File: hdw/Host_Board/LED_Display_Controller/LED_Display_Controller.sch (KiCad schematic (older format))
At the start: 0 parts

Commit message: I said never do this, it's bad for you
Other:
- note added: "To Do List:\n* Add voltage rail ADC dividers/filters\n* ESD protection on input and output signals\n* Add graphical items to certain sheets (ESD warning, heat, etc)\n* Add MU Logo to each sheet\n* Add Titles to each sheet\n* Add relevant design notes/routing notes to sheets\n* Add test points sheet\n* Re-order sheets\n* Wire everything to Micro\n* Assign Refdes's\n* Draw custom footprints\n* Assi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"
- note removed: "To Do List:\n* Mechanical sheet\n* Decide on input power supply (AC/DC)\n* Add more power input connectors, match to AC/DC output connectors. Might need beefy Wuerth shanks\n* Add status LEDs, PGOOD stuff\n* +3.3V Power Supply (~~2A)\n* Add AUX +5V input if we mess up +5V supply\n* Wi-Fi Module\n* Evaluate Micro AVDD/AVSS filter\n* Power pushbutton? vs set on app?\n* Brightness encoder? vs set on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"
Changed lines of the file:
@@
 $Descr A 11000 8500
 encoding utf-8
-Sheet 1 32
+Sheet 1 31
 Title ""
 Date ""
@@
 F0 "Panel Data Connectors" 50
 F1 "Panel_Data_Connectors.sch" 50
-$EndSheet
-$Sheet
-S 3050 3270 500  150
-U 5BAAE2DF
-F0 "Panel Power Connectors" 50
-F1 "Panel_Power_Connectors.sch" 50
 $EndSheet
 $Sheet
@@
 $EndSheet
 Text Notes 710  7660 0    50   ~ 0
-To Do List:\n* Mechanical sheet\n* Decide on input power supply (AC/DC)\n* Add more power input connectors, match to AC/DC output connectors. Might need beefy Wuerth shanks\n* Add status LEDs, PGOOD stuff\n* +3.3V Power Supply (~~2A)\n* Add AUX +5V input if we mess up +5V supply\n* Wi-Fi Module\n* Evaluate Micro AVDD/AVSS filter\n* Power pushbutton? vs set on app?\n* Brightness encoder? vs set on app?\n* Add graphical items to certain sheets (ESD warning, heat, etc)\n* Add MU Logo to each sheet\n* Add Titles to each sheet\n* Add relevant design notes/routing notes to sheets\n* Add test points sheet\n* Re-order sheets\n* Wire everything to Micro\n* Assign Refdes's\n* Draw custom footprints\n* Assign footprints\n* Run ERC, resolve errors\n* Add firmware notes sheet\n* Add COM port settings note to USB sheet\n* Generate netlist\n* Generate BOM
+To Do List:\n* Add voltage rail ADC dividers/filters\n* ESD protection on input and output signals\n* Add graphical items to certain sheets (ESD warning, heat, etc)\n* Add MU Logo to each sheet\n* Add Titles to each sheet\n* Add relevant design notes/routing notes to sheets\n* Add test points sheet\n* Re-order sheets\n* Wire everything to Micro\n* Assign Refdes's\n* Draw custom footprints\n* Assign footprints\n* Assign Digi-Key Partnumbers\n* Run ERC, resolve errors\n* Add firmware notes sheet\n* Add COM port settings notes to USB sheet\n* Generate netlist\n* Generate BOM\n* Layout PCB
 $Sheet
 S 5450 5360 500  150
@@
 $EndSheet
 $Sheet
-S 7300 770  500  150
-U 5BC2370E
-F0 "POS5 Control" 50
-F1 "POS5_Control.sch" 50
+S 3050 3290 500  150
+U 5BE48F98
+F0 "LED POS5 Monitoring" 50
+F1 "LED_POS5_Monitoring.sch" 50
 $EndSheet
 $Sheet
-S 7300 1090 500  150
-U 5BC23711
-F0 "POS5 Phase 1" 50
-F1 "POS5_Phase_1.sch" 50
+S 5450 5700 500  150
+U 5BE4F849
+F0 "Pushbuttons" 50
+F1 "Pushbuttons.sch" 50
 $EndSheet
 $Sheet
-S 7300 1400 500  150
-U 5BC23715
-F0 "POS5 Phase 2" 50
-F1 "POS5_Phase_2.sch" 50
+S 5450 6040 500  150
+U 5BE5222A
+F0 "POS5 Power Supply" 50
+F1 "POS5_Power_Supply.sch" 50
 $EndSheet
 $Sheet
-S 7300 1740 500  150
-U 5BC2371A
-F0 "POS5 Phase 3" 50
-F1 "POS5_Phase_3.sch" 50
+S 7070 800  500  150
+U 5BE724F0
+F0 "Mechanical" 50
+F1 "Mechanical.sch" 50
 $EndSheet
 $Sheet
-S 7300 2060 500  150
-U 5BC2371D
-F0 "POS5 Phase 4" 50
-F1 "POS5_Phase_4.sch" 50
+S 7070 1140 500  150
+U 5BE7BB83
+F0 "Internal Rail Monitoring" 50
+F1 "Internal_Rail_Monitoring.sch" 50
 $EndSheet
 $Sheet
-S 7300 2430 500  150
-U 5BC23720
-F0 "POS5P5 MNG" 50
-F1 "POS5P5_MNG.sch" 50
+S 7070 1480 500  150
+U 5BF346B3
+F0 "Status LEDs 2" 50
+F1 "Status_LEDs_2.sch" 50
 $EndSheet
 $EndSCHEMATC

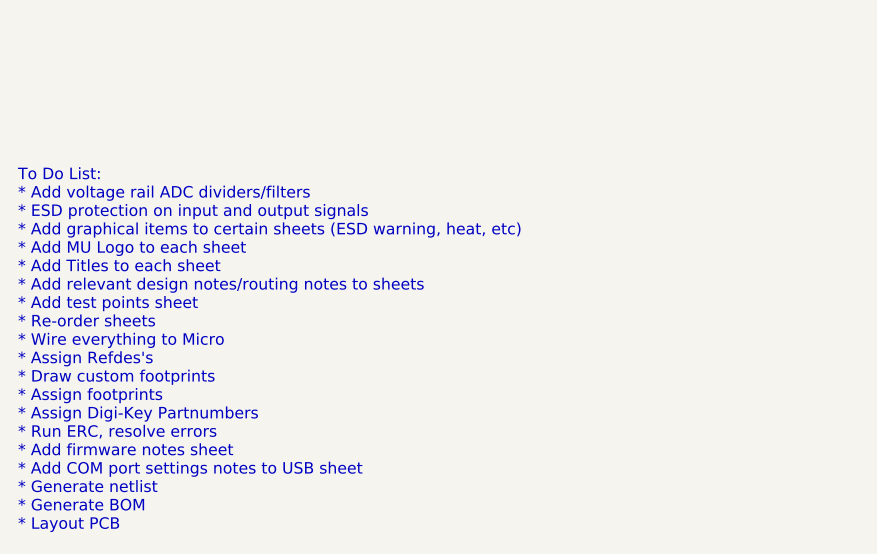
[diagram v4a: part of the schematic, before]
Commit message: Wired a lot of signals to micro, added COM port notes
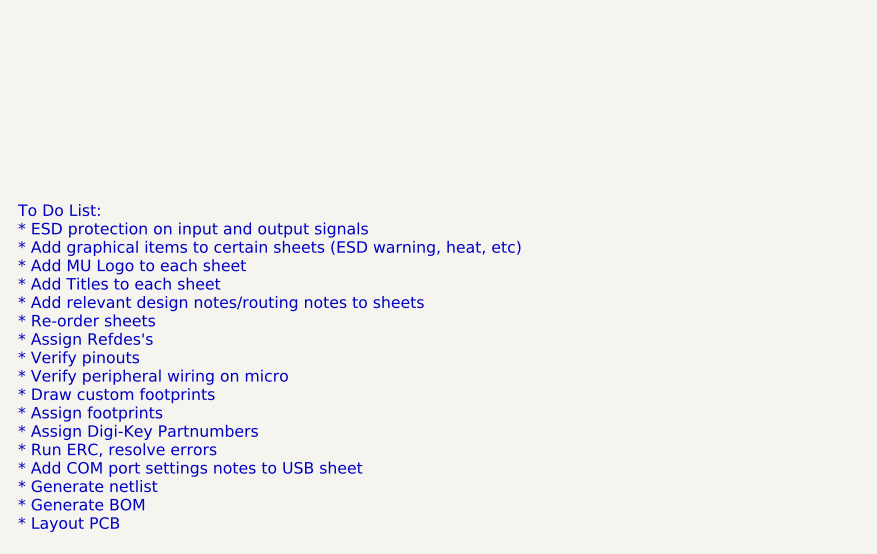
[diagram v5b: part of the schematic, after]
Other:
- note added: "To Do List:\n* ESD protection on input and output signals\n* Add graphical items to certain sheets (ESD warning, heat, etc)\n* Add MU Logo to each sheet\n* Add Titles to each sheet\n* Add relevant design notes/routing notes to sheets\n* Re-order sheets\n* Assign Refdes's\n* Verify pinouts\n* Verify peripheral wiring on micro\n* Draw custom footprints\n* Assign footprints\n* Assign Digi-Key Partnu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"
- note removed: "To Do List:\n* Add voltage rail ADC dividers/filters\n* ESD protection on input and output signals\n* Add graphical items to certain sheets (ESD warning, heat, etc)\n* Add MU Logo to each sheet\n* Add Titles to each sheet\n* Add relevant design notes/routing notes to sheets\n* Add test points sheet\n* Re-order sheets\n* Wire everything to Micro\n* Assign Refdes's\n* Draw custom footprints\n* Assi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"
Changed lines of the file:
@@
 $EndSheet
 Text Notes 710  7660 0    50   ~ 0
-To Do List:\n* Add voltage rail ADC dividers/filters\n* ESD protection on input and output signals\n* Add graphical items to certain sheets (ESD warning, heat, etc)\n* Add MU Logo to each sheet\n* Add Titles to each sheet\n* Add relevant design notes/routing notes to sheets\n* Add test points sheet\n* Re-order sheets\n* Wire everything to Micro\n* Assign Refdes's\n* Draw custom footprints\n* Assign footprints\n* Assign Digi-Key Partnumbers\n* Run ERC, resolve errors\n* Add firmware notes sheet\n* Add COM port settings notes to USB sheet\n* Generate netlist\n* Generate BOM\n* Layout PCB
+To Do List:\n* ESD protection on input and output signals\n* Add graphical items to certain sheets (ESD warning, heat, etc)\n* Add MU Logo to each sheet\n* Add Titles to each sheet\n* Add relevant design notes/routing notes to sheets\n* Re-order sheets\n* Assign Refdes's\n* Verify pinouts\n* Verify peripheral wiring on micro\n* Draw custom footprints\n* Assign footprints\n* Assign Digi-Key Partnumbers\n* Run ERC, resolve errors\n* Add COM port settings notes to USB sheet\n* Generate netlist\n* Generate BOM\n* Layout PCB
 $Sheet
 S 5450 5360 500  150

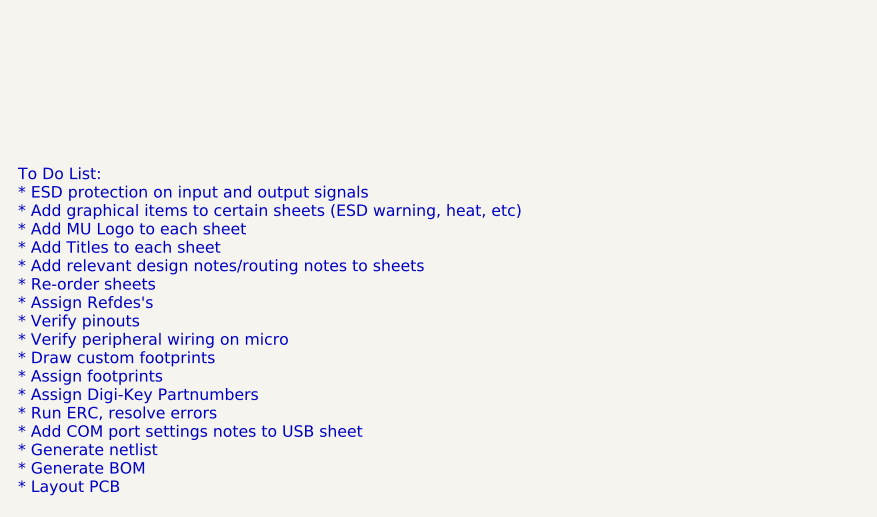
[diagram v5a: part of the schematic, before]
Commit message: Added graphical symbols to certain sheets
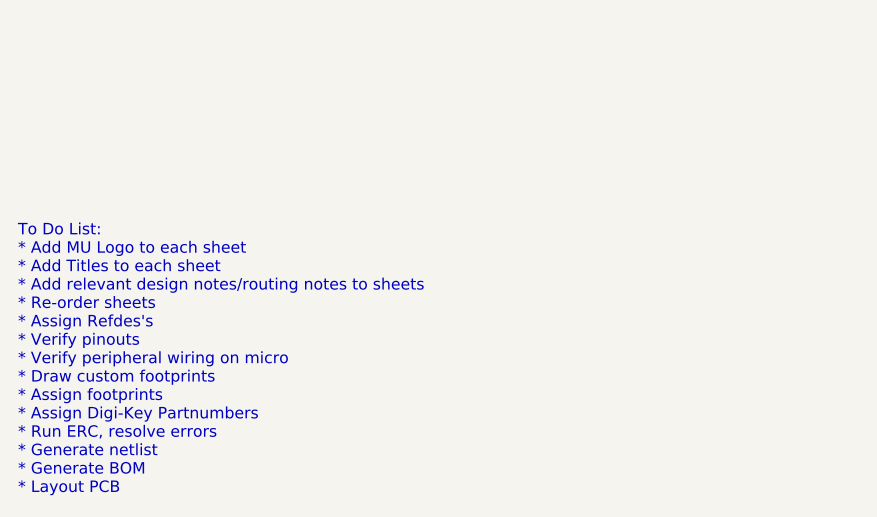
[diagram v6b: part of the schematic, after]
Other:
- note added: "To Do List:\n* Add MU Logo to each sheet\n* Add Titles to each sheet\n* Add relevant design notes/routing notes to sheets\n* Re-order sheets\n* Assign Refdes's\n* Verify pinouts\n* Verify peripheral wiring on micro\n* Draw custom footprints\n* Assign footprints\n* Assign Digi-Key Partnumbers\n* Run ERC, resolve errors\n* Generate netlist\n* Generate BOM\n* Layout PCB"
- note removed: "To Do List:\n* ESD protection on input and output signals\n* Add graphical items to certain sheets (ESD warning, heat, etc)\n* Add MU Logo to each sheet\n* Add Titles to each sheet\n* Add relevant design notes/routing notes to sheets\n* Re-order sheets\n* Assign Refdes's\n* Verify pinouts\n* Verify peripheral wiring on micro\n* Draw custom footprints\n* Assign footprints\n* Assign Digi-Key Partnu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"
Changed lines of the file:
@@
 $EndSheet
 Text Notes 710  7660 0    50   ~ 0
-To Do List:\n* ESD protection on input and output signals\n* Add graphical items to certain sheets (ESD warning, heat, etc)\n* Add MU Logo to each sheet\n* Add Titles to each sheet\n* Add relevant design notes/routing notes to sheets\n* Re-order sheets\n* Assign Refdes's\n* Verify pinouts\n* Verify peripheral wiring on micro\n* Draw custom footprints\n* Assign footprints\n* Assign Digi-Key Partnumbers\n* Run ERC, resolve errors\n* Add COM port settings notes to USB sheet\n* Generate netlist\n* Generate BOM\n* Layout PCB
+To Do List:\n* Add MU Logo to each sheet\n* Add Titles to each sheet\n* Add relevant design notes/routing notes to sheets\n* Re-order sheets\n* Assign Refdes's\n* Verify pinouts\n* Verify peripheral wiring on micro\n* Draw custom footprints\n* Assign footprints\n* Assign Digi-Key Partnumbers\n* Run ERC, resolve errors\n* Generate netlist\n* Generate BOM\n* Layout PCB
 $Sheet
 S 5450 5360 500  150

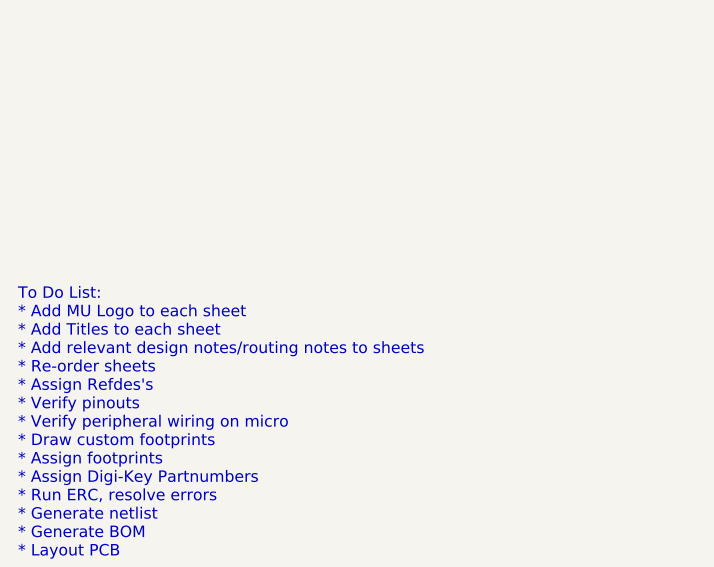
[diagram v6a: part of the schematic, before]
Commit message: Added item to to do list
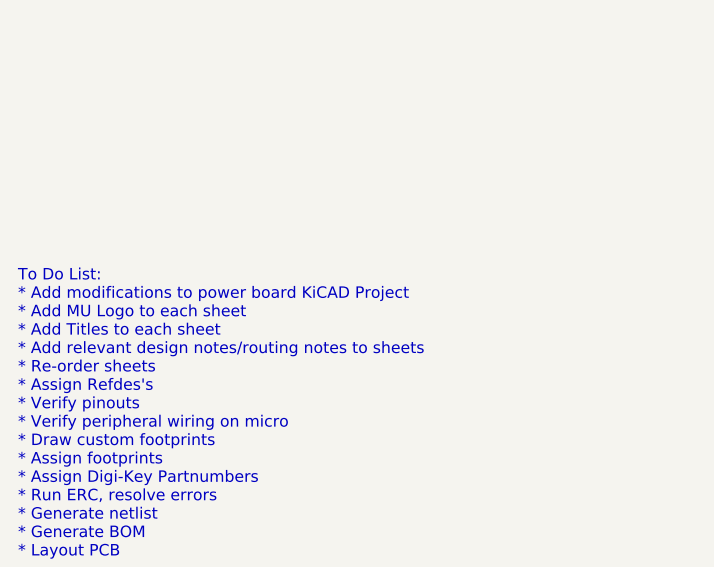
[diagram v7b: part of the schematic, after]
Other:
- note added: "To Do List:\n* Add modifications to power board KiCAD Project\n* Add MU Logo to each sheet\n* Add Titles to each sheet\n* Add relevant design notes/routing notes to sheets\n* Re-order sheets\n* Assign Refdes's\n* Verify pinouts\n* Verify peripheral wiring on micro\n* Draw custom footprints\n* Assign footprints\n* Assign Digi-Key Partnumbers\n* Run ERC, resolve errors\n* Generate netlist\n* Genera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"
- note removed: "To Do List:\n* Add MU Logo to each sheet\n* Add Titles to each sheet\n* Add relevant design notes/routing notes to sheets\n* Re-order sheets\n* Assign Refdes's\n* Verify pinouts\n* Verify peripheral wiring on micro\n* Draw custom footprints\n* Assign footprints\n* Assign Digi-Key Partnumbers\n* Run ERC, resolve errors\n* Generate netlist\n* Generate BOM\n* Layout PCB"
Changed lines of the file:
@@
 $EndSheet
 Text Notes 710  7660 0    50   ~ 0
-To Do List:\n* Add MU Logo to each sheet\n* Add Titles to each sheet\n* Add relevant design notes/routing notes to sheets\n* Re-order sheets\n* Assign Refdes's\n* Verify pinouts\n* Verify peripheral wiring on micro\n* Draw custom footprints\n* Assign footprints\n* Assign Digi-Key Partnumbers\n* Run ERC, resolve errors\n* Generate netlist\n* Generate BOM\n* Layout PCB
+To Do List:\n* Add modifications to power board KiCAD Project\n* Add MU Logo to each sheet\n* Add Titles to each sheet\n* Add relevant design notes/routing notes to sheets\n* Re-order sheets\n* Assign Refdes's\n* Verify pinouts\n* Verify peripheral wiring on micro\n* Draw custom footprints\n* Assign footprints\n* Assign Digi-Key Partnumbers\n* Run ERC, resolve errors\n* Generate netlist\n* Generate BOM\n* Layout PCB
 $Sheet
 S 5450 5360 500  150

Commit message: Cleaned up a few sheets
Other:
- note added: "To Do List:\n* Add modifications to power board KiCAD Project\n* Add MU Logo to each sheet\n* Add Titles to each sheet\n* Re-order sheets\n* Assign Refdes's\n* Verify pinouts\n* Verify peripheral wiring on micro\n* Draw custom footprints\n* Assign footprints\n* Assign Digi-Key Partnumbers\n* Run ERC, resolve errors\n* Generate netlist\n* Generate BOM\n* Layout PCB"
- note removed: "To Do List:\n* Add modifications to power board KiCAD Project\n* Add MU Logo to each sheet\n* Add Titles to each sheet\n* Add relevant design notes/routing notes to sheets\n* Re-order sheets\n* Assign Refdes's\n* Verify pinouts\n* Verify peripheral wiring on micro\n* Draw custom footprints\n* Assign footprints\n* Assign Digi-Key Partnumbers\n* Run ERC, resolve errors\n* Generate netlist\n* Genera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"
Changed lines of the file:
@@
 $EndSheet
 Text Notes 710  7660 0    50   ~ 0
-To Do List:\n* Add modifications to power board KiCAD Project\n* Add MU Logo to each sheet\n* Add Titles to each sheet\n* Add relevant design notes/routing notes to sheets\n* Re-order sheets\n* Assign Refdes's\n* Verify pinouts\n* Verify peripheral wiring on micro\n* Draw custom footprints\n* Assign footprints\n* Assign Digi-Key Partnumbers\n* Run ERC, resolve errors\n* Generate netlist\n* Generate BOM\n* Layout PCB
+To Do List:\n* Add modifications to power board KiCAD Project\n* Add MU Logo to each sheet\n* Add Titles to each sheet\n* Re-order sheets\n* Assign Refdes's\n* Verify pinouts\n* Verify peripheral wiring on micro\n* Draw custom footprints\n* Assign footprints\n* Assign Digi-Key Partnumbers\n* Run ERC, resolve errors\n* Generate netlist\n* Generate BOM\n* Layout PCB
 $Sheet
 S 5450 5360 500  150
